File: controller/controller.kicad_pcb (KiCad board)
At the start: 2 copper layers, 69.6 x 37.3 mm, 46 parts, among them J1 Conn_01x25_Membrane, J2 Conn_01x04, SW1 SW_Push, SW2 SW_Push, U1 AMS1117-3.3, U2 STM32F303RCT6, U3 TPS2553DBVR, U4 USBLC6-2SC6, Y1 16MHz

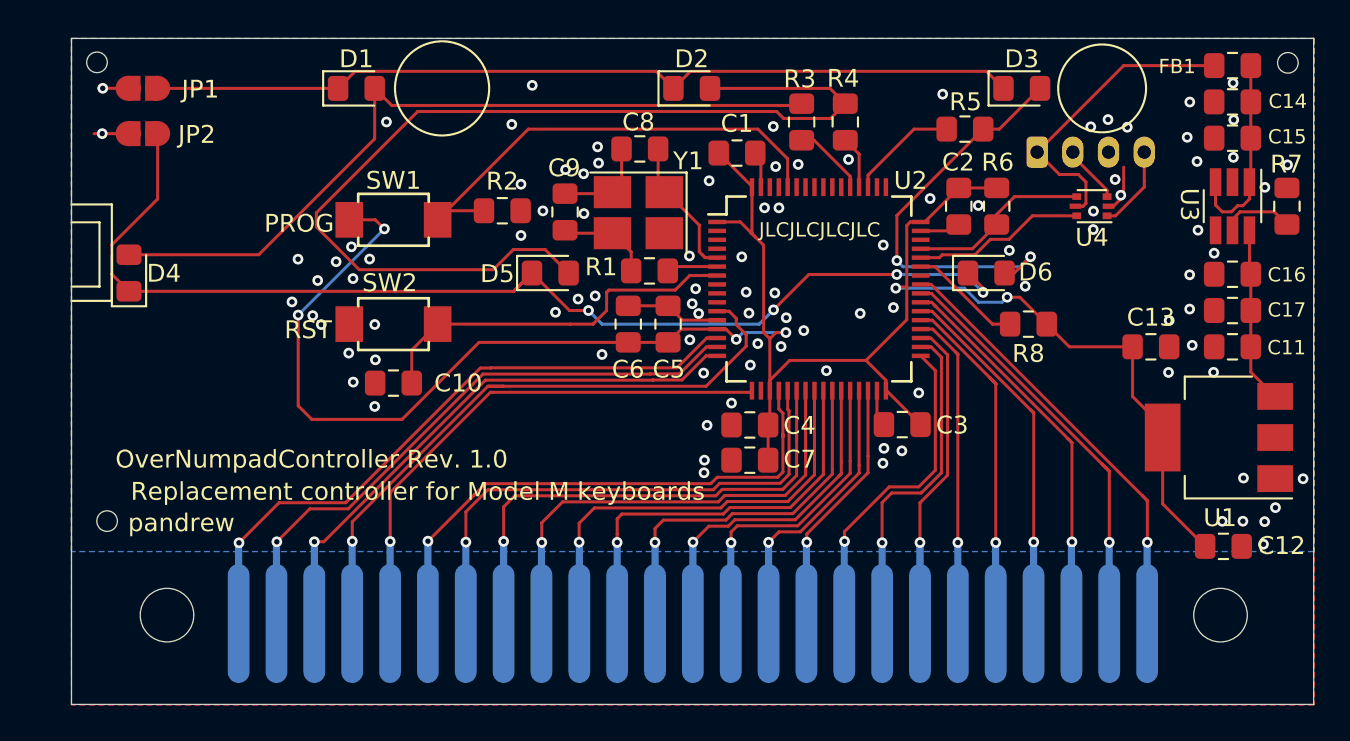
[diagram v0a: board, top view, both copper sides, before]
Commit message: added solenoid driver
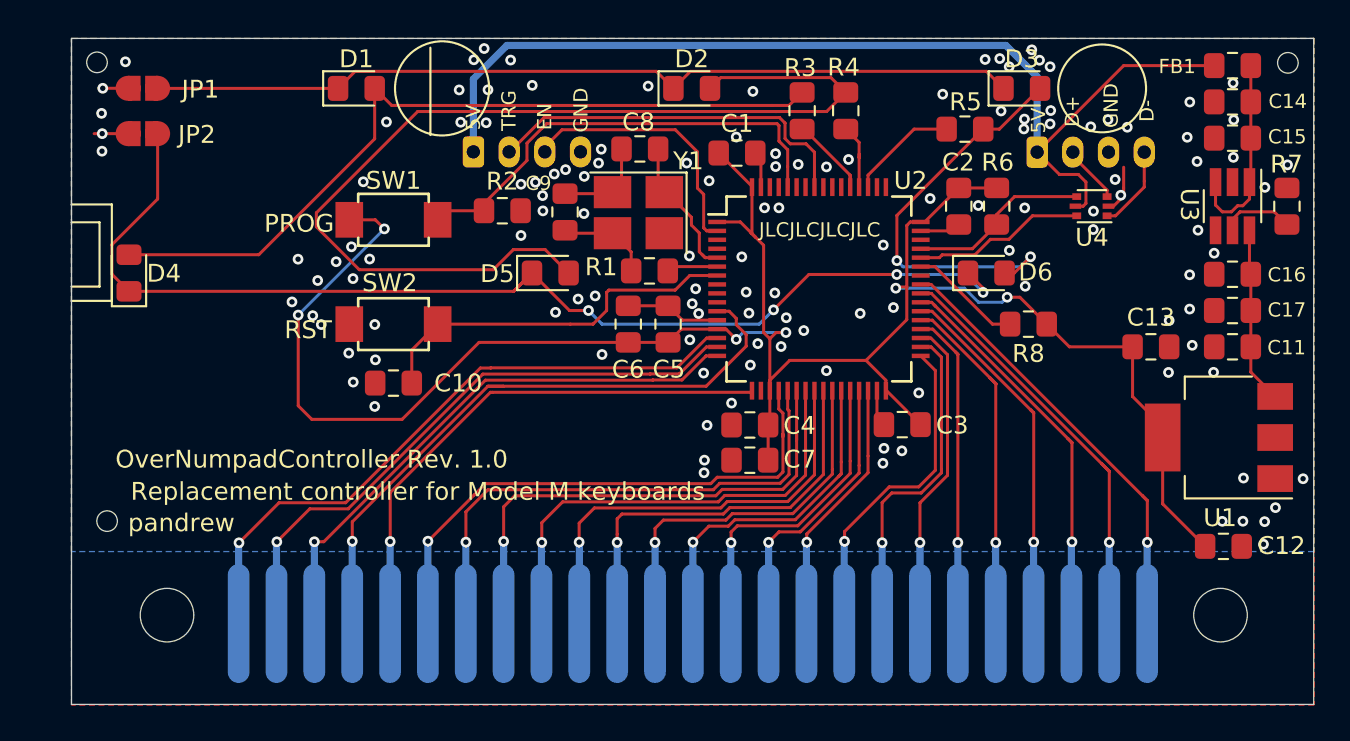
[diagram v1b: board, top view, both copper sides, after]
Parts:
- added J3: Conn_Solenoid_Driver, Connector_JST:JST_PH_S4B-PH-K_1x04_P2.00mm_Horizontal, B.Cu at (86.5, 138.4)
- moved R3 0.63 mm to (104.9, 136.1)
- moved R4 0.63 mm to (107.4, 136.1)
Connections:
- U2 pad 2: Net-(U2-Pad2) -> SOLENOID_ENABLE
- U2 pad 57: Net-(U2-Pad57) -> SOLENOID_TRIGGER
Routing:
- net VBUS: track 17.2 -> 58.6 mm
- net SOLENOID_TRIGGER: track 0.00 -> 21.2 mm
- net SOLENOID_ENABLE: track 0.00 -> 15.0 mm
- net Net-(R2-Pad1): track 26.8 -> 25.8 mm
- net LEDDRV1: track 4.16 -> 5.04 mm
- net LEDDRV2: track 2.95 -> 3.76 mm
- net GND: vias 100 -> 130
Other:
- board text added: "5V"
- board text added: "D+"
- board text added: "D-"
- board text added: "EN"
- board text added: "GND"
- board text added: "SOLENOID DRIVER"
- board text added: "TRG"
- board text added: "USB"

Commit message: added gpio header and other updates
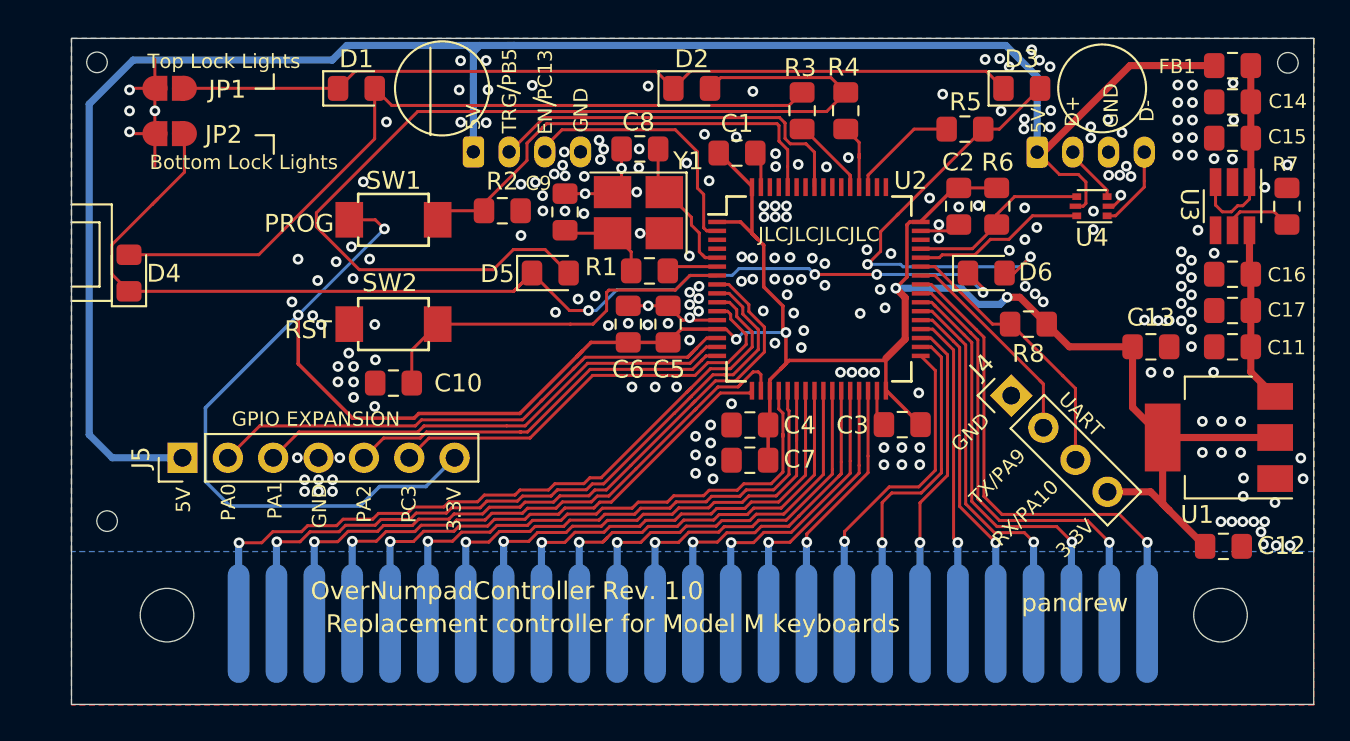
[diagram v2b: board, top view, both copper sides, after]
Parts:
- added J4: Conn_01x04, Connector_PinHeader_2.54mm:PinHeader_1x04_P2.54mm_Vertical, F.Cu at (116.6, 152.1)
- added J5: Conn_01x07, Connector_PinHeader_2.54mm:PinHeader_1x07_P2.54mm_Vertical, F.Cu at (70.2, 155.6)
- moved JP1 1.50 mm to (69.5, 134.9)
- moved JP2 1.50 mm to (69.5, 137.4)
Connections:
- net Net-(R8-Pad2) renamed UART_RX
- U2 pad 10: Net-(U2-Pad10) -> MEMBRANE25
- U2 pad 11: MEMBRANE22 -> GPIO_PC3
- U2 pad 14: MEMBRANE25 -> GPIO_PA0
- U2 pad 15: MEMBRANE24 -> GPIO_PA1
- U2 pad 16: MEMBRANE23 -> GPIO_PA2
- U2 pad 18: Net-(U2-Pad18) -> MEMBRANE22
- U2 pad 42: Net-(U2-Pad42) -> UART_TX
- U2 pad 8: Net-(U2-Pad8) -> MEMBRANE23
- U2 pad 9: Net-(U2-Pad9) -> MEMBRANE24
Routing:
- net VBUS: track 58.6 -> 107.9 mm
- net +3.3VA: track 120.4 -> 156.4 mm
- net GPIO_PA0: track 0.00 -> 31.6 mm
- net GPIO_PA1: track 0.00 -> 27.4 mm
- net GPIO_PC3: track 0.00 -> 24.4 mm
- net GPIO_PA2: track 0.00 -> 22.1 mm
- net UART_TX: track 0.00 -> 12.1 mm
- net UART_RX: track 6.34 -> 15.7 mm
- net MEMBRANE23: track 31.5 -> 39.7 mm
- net MEMBRANE24: track 33.8 -> 40.7 mm
- net MEMBRANE25: track 36.1 -> 42.5 mm
- net GND: track 23.3 -> 27.0 mm, vias 130 -> 228
- net MEMBRANE1: track 25.0 -> 28.5 mm
- net MEMBRANE22: track 35.7 -> 32.5 mm
- net Net-(D3-Pad2): track 23.2 -> 25.7 mm
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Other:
- board text added: "3.3V"
- board text added: "Bottom Lock Lights"
- board text added: "GPIO EXPANSION"
- board text added: "PA0"
- board text added: "PA1"
- board text added: "PA2"
- board text added: "PB5"
- board text added: "PC13"
- board text added: "PC3"
- board text added: "RX/PA10"
- board text added: "SOLENOID EXPANSION"
- board text added: "TX/PA9"
- board text added: "Top Lock Lights"
- board text added: "UART"
- board text removed: "SOLENOID DRIVER"

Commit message: LED current limit resistors changed to 47 ohm
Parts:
- R3, R4, R5: value 330 -> 47

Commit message: more updates
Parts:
- added J6: Conn_01x06, Connector_PinHeader_1.27mm:PinHeader_1x06_P1.27mm_Vertical, F.Cu at (109.6, 137.8)
- moved R5 3.88 mm to (110.7, 135.1)
- moved J2 0.70 mm to (118.8, 138.4)
- moved J4 0.20 mm to (116.8, 152.1)
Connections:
- U2 pad 49: Net-(U2-Pad49) -> GPIO_PA14
- U2 pad 50: Net-(U2-Pad50) -> GPIO_PA15
- U2 pad 54: Net-(U2-Pad54) -> GPIO_PD2
- U2 pad 55: Net-(U2-Pad55) -> GPIO_PB3
- U2 pad 56: Net-(U2-Pad56) -> GPIO_PB4
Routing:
- net GPIO_PB4: track 0.00 -> 12.6 mm
- net GPIO_PB3: track 0.00 -> 10.6 mm
- net GPIO_PD2: track 0.00 -> 8.07 mm
- net Net-(D3-Pad2): track 25.7 -> 33.3 mm
- net VBUS: track 107.9 -> 113.2 mm, vias 0 -> 2
- net GPIO_PA14: track 0.00 -> 3.11 mm
- net GPIO_PA15: track 0.00 -> 2.79 mm
- net USB_DM_ESD: track 4.70 -> 5.88 mm
- net GND: track 27.0 -> 27.4 mm, vias 228 -> 223
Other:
- board text added: "PA14"
- board text added: "PA15"
- board text added: "PB3"
- board text added: "PB4"
- board text added: "PD2"
